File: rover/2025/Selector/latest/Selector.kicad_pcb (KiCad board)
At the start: 4 copper layers, 51 x 47.5 mm, 18 parts, among them J2 JST4_Pin, J3 JST6_Pin, J4 JST3_Pin, J5 JST3_Pin, J6 JST2_Pin, U1 XT60PW-M

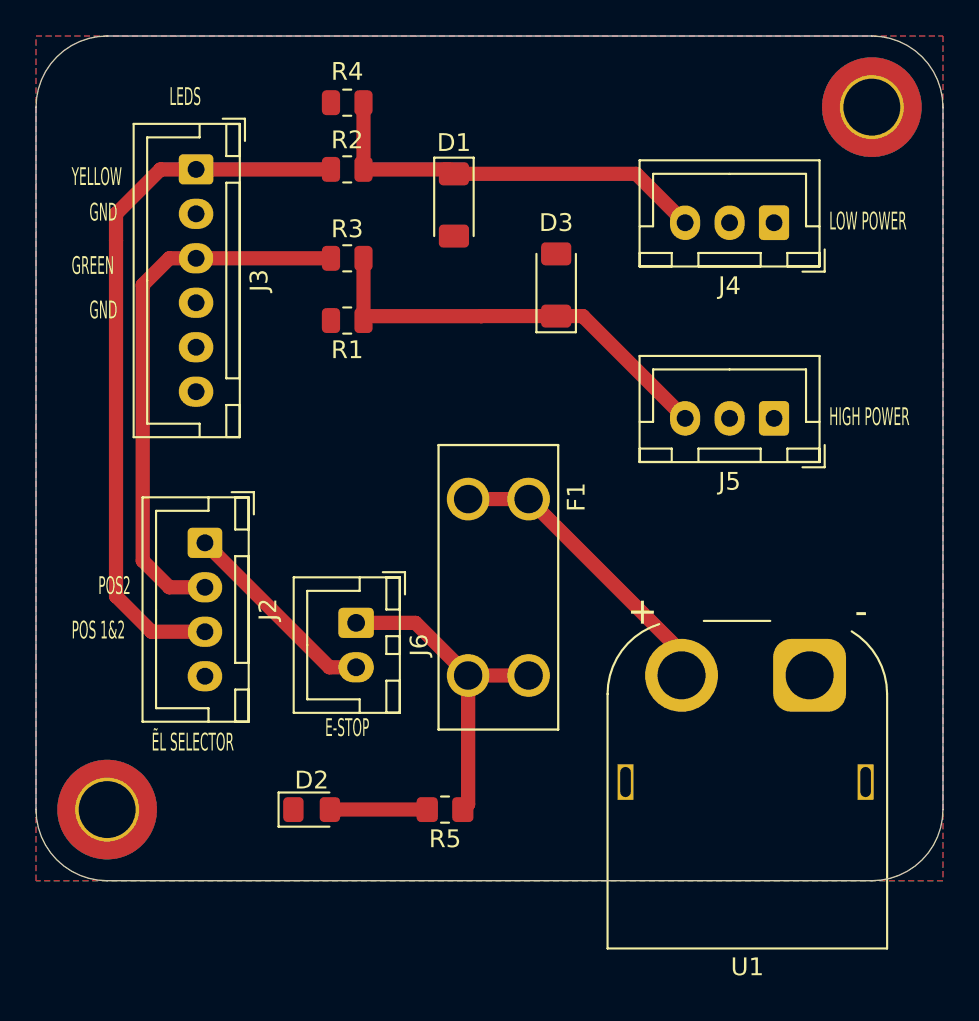
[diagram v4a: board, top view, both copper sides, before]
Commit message: Selector JST PH connectors
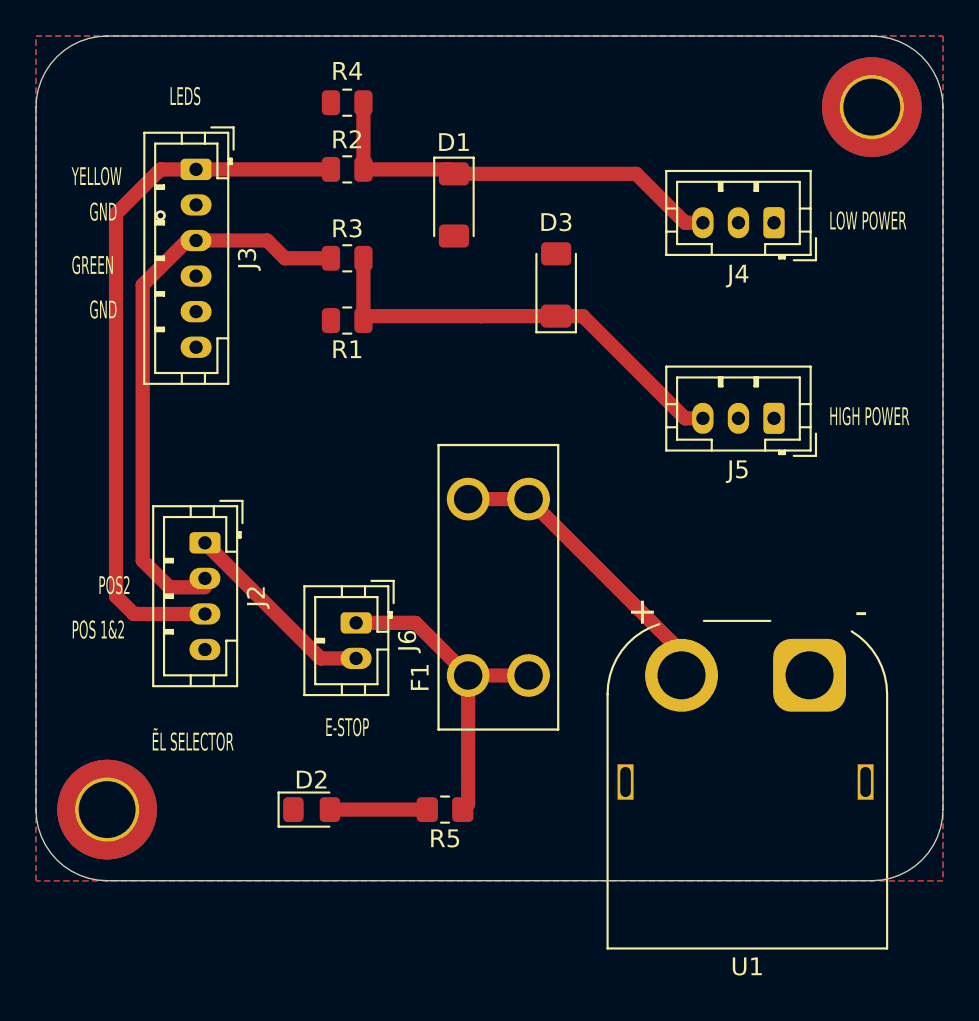
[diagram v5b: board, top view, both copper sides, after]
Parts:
- J2: footprint Connector_JST:JST_XH_B4B-XH-A_1x04_P2.50mm_Vertical -> Connector_JST:JST_PH_B4B-PH-K_1x04_P2.00mm_Vertical
- J3: footprint Connector_JST:JST_XH_B6B-XH-A_1x06_P2.50mm_Vertical -> Connector_JST:JST_PH_B6B-PH-K_1x06_P2.00mm_Vertical
- J4, J5: footprint Connector_JST:JST_XH_B3B-XH-A_1x03_P2.50mm_Vertical -> Connector_JST:JST_PH_B3B-PH-K_1x03_P2.00mm_Vertical
- J6: footprint RoverFootprint:2-pins-JST_XH_B2B-XH-A_1x02_P2.50mm_Vertical -> Connector_JST:JST_PH_B2B-PH-K_1x02_P2.00mm_Vertical
- turned F1 to 90 degrees
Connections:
- F1 pad 1: Net-(U1-+) -> +24V
- F1 pad 2: +24V -> Net-(U1-+)
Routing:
- net Net-(D3-K): track 24.1 -> 25.1 mm
- net Net-(D1-K): track 22.5 -> 23.5 mm
- net POS2: track 30.8 -> 31.7 mm
- net GND: vias 0 -> 1
